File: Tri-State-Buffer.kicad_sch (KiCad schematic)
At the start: 22 parts, among them J1 Conn_01x08, J2 Conn_01x08

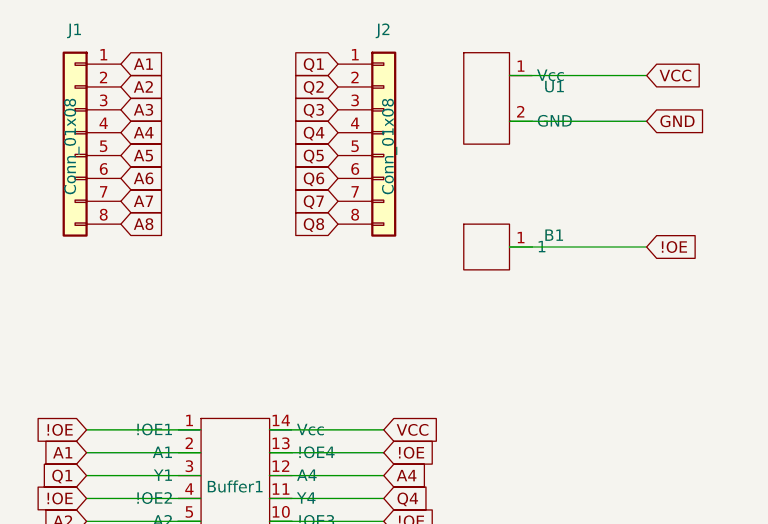
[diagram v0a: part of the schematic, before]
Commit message: Added Mounting Holes
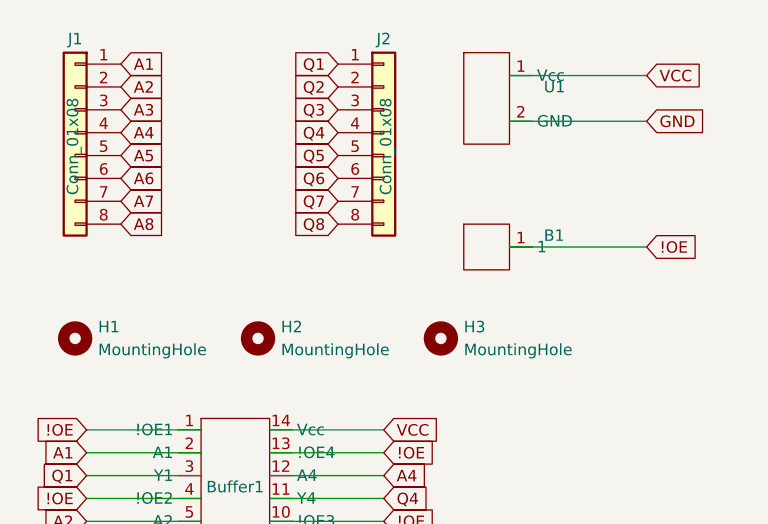
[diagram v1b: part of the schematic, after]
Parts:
- added H1, H2, H3: MountingHole, MountingHole:MountingHole_2.1mm, symbol Mechanical:MountingHole
- J1, J2: footprint (none) -> Connector_PinHeader_2.54mm:PinHeader_1x08_P2.54mm_Vertical
